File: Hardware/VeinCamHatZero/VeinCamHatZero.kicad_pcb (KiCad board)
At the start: 2 copper layers, 65 x 30 mm, 17 parts, among them J1 Raspberry_Pi_2_3, Q1 BSD235N

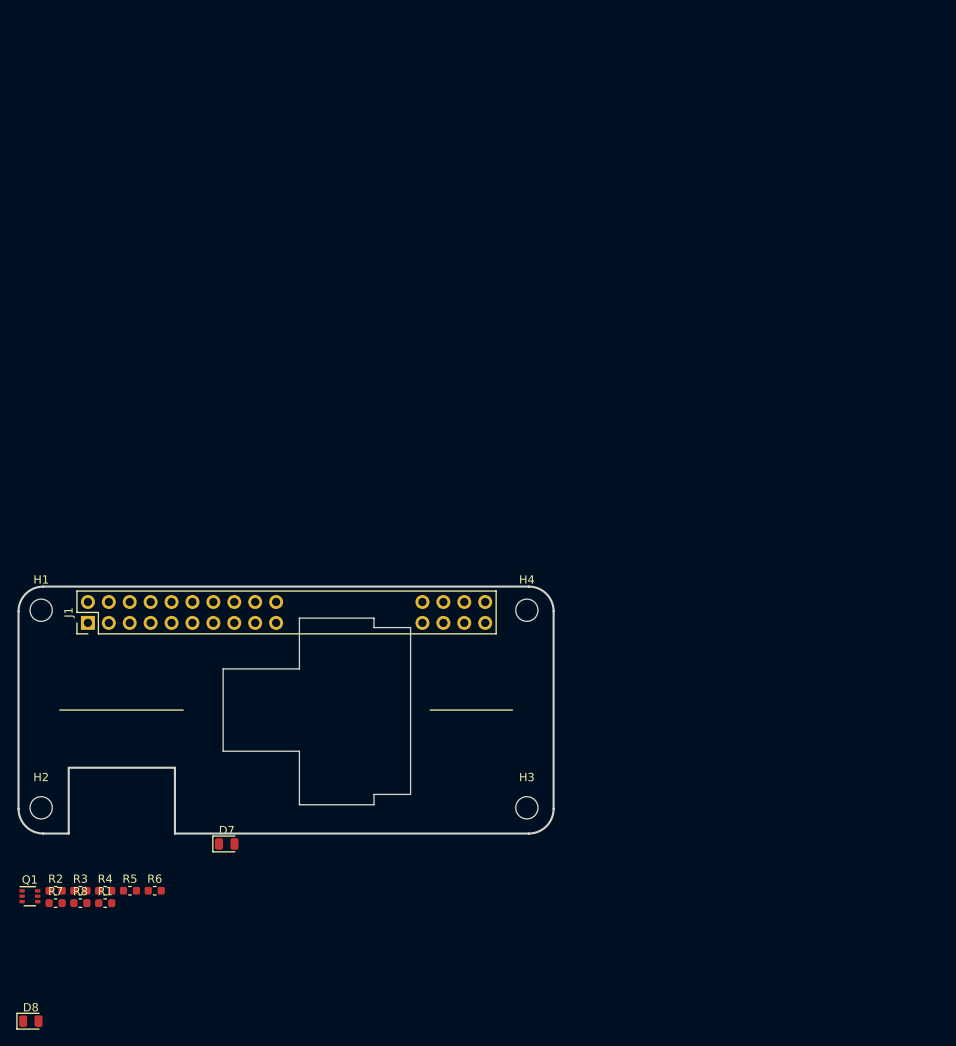
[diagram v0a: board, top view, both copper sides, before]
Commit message: Laid out VeinCamHatZero and added IR LED footprint/model
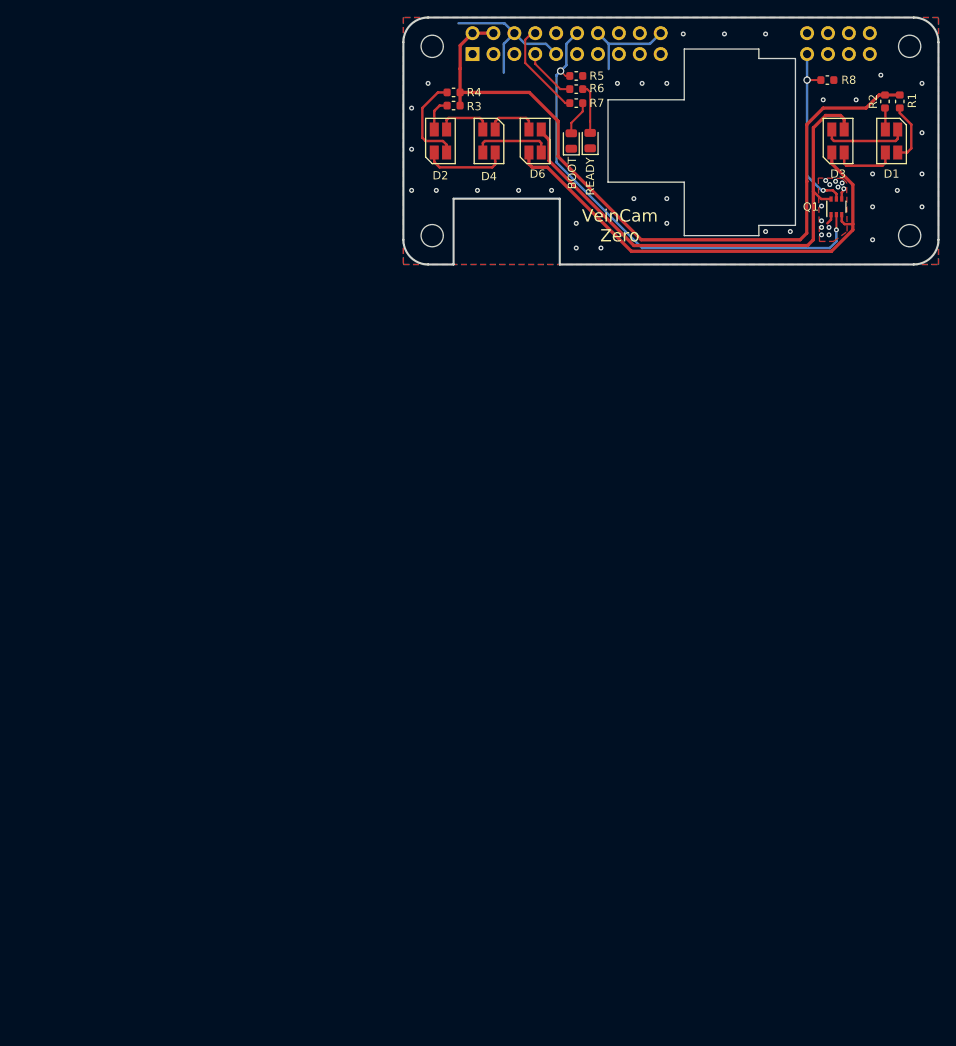
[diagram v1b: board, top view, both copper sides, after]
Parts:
- added D1: SFH7252, VeinCam_Footprints:SFH7252, F.Cu at (264.3, 80.0)
- added D2: SFH7252, VeinCam_Footprints:SFH7252, F.Cu at (209.5, 80.0)
- added D3: SFH7252, VeinCam_Footprints:SFH7252, F.Cu at (257.8, 80.0)
- added D4: SFH7252, VeinCam_Footprints:SFH7252, F.Cu at (215.4, 80.0)
- added D6: SFH7252, VeinCam_Footprints:SFH7252, F.Cu at (221.0, 80.0)
- moved R2 139.1 mm to (263.5, 75.2), turned to 90 degrees
- moved R1 137.1 mm to (265.3, 75.2), turned to 90 degrees
- moved R8 135.0 mm to (256.5, 72.6)
- moved Q1 128.9 mm to (257.6, 88.0), turned to 90 degrees
- moved D8 125.5 mm to (225.4, 80.0), turned to 90 degrees
- moved R7 116.0 mm to (226.0, 75.4)
- moved R5 112.9 mm to (226.0, 72.1)
- moved R6 110.0 mm to (226.0, 73.7)
- moved R4 105.8 mm to (211.1, 74.1)
- moved R3 105.6 mm to (211.1, 75.7)
- moved D7 96.2 mm to (227.7, 80.0), turned to 90 degrees
- moved H2 84.2 mm to (208.5, 91.5)
- moved H3 83.6 mm to (266.5, 91.5)
- moved TP1 83.5 mm to (205.0, 95.0)
- moved J1 83.4 mm to (213.4, 69.4)
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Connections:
- J1 pad 1: +3V3 -> Net-(J1-Pad1)
- J1 pad 12: Net-(J1-Pad12) -> /LED_940
- J1 pad 15: /LED_READY -> Net-(J1-Pad15)
- J1 pad 16: /LED_BOOT -> Net-(J1-Pad16)
- J1 pad 17: +3V3 -> Net-(J1-Pad17)
- J1 pad 7: Net-(J1-Pad7) -> /LED_READY
- J1 pad 8: Net-(J1-Pad8) -> /LED_BOOT
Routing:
- net +5V: track 0.00 -> 90.3 mm
- net Net-(D3-Pad3): track 0.00 -> 62.8 mm
- net /LED_940: track 0.00 -> 60.0 mm, vias 0 -> 2
- net Net-(D3-Pad1): track 0.00 -> 59.0 mm
- net GND: track 0.00 -> 33.0 mm, vias 0 -> 45
- net /LED_850: track 0.00 -> 21.6 mm, vias 0 -> 2
- net /LED_BOOT: track 0.00 -> 11.8 mm
- net Net-(D2-Pad4): track 0.00 -> 11.7 mm
- net Net-(D2-Pad1): track 0.00 -> 10.5 mm
- net Net-(D1-Pad1): track 0.00 -> 10.5 mm
- net Net-(D4-Pad3): track 0.00 -> 9.61 mm
- net Net-(D1-Pad3): track 0.00 -> 8.22 mm
- net Net-(D1-Pad2): track 0.00 -> 7.35 mm
- net Net-(D2-Pad3): track 0.00 -> 6.85 mm
- net /LED_READY: track 0.00 -> 6.66 mm
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- added copper zone on B.Cu, net GND
- added copper zone on F.Cu, net GND
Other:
- rule via_min_drill: 0.5 -> 0.3
- rule via_min_size: 0.8 -> 0.6
- board text added: "Alex Binos Chris Bodger Josh Johnson Tom Johnson Alex Ollman Pat Wilton"
- board text added: "BOOT"
- board text added: "READY"
- board text added: "VeinCam Zero"
- board text added: "VeinCam2019:"
- board text added: "github.com/chrisbodger/VeinCam2019"

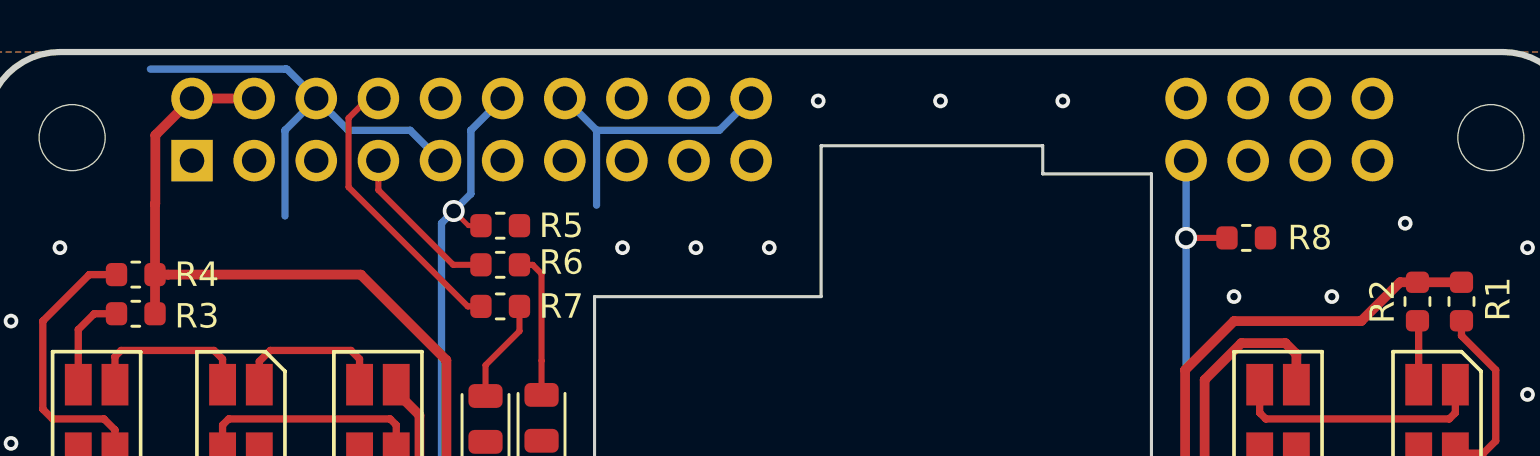
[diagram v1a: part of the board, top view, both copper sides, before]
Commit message: Added footprints for VeinCamHat and begun layout
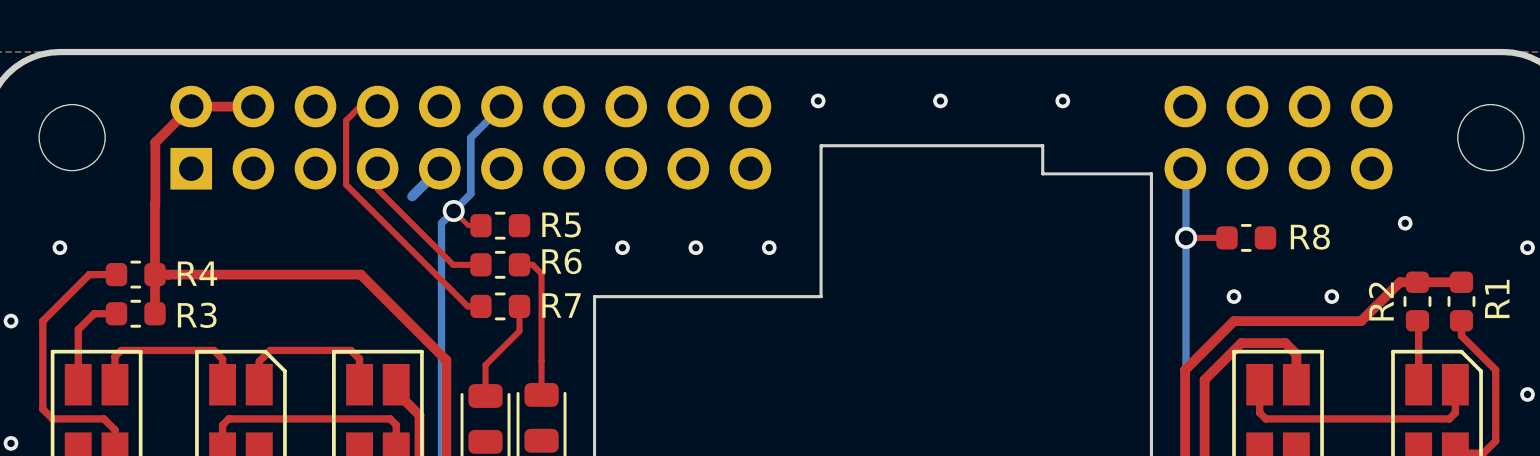
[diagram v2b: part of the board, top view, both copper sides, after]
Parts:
- moved J1 0.33 mm to (213.4, 69.8)
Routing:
- net GND: track 33.0 -> 4.15 mm

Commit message: Changes to renders
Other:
- board text added: "VeinCam"
- board text removed: "VeinCam Zero"
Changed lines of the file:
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@@
     (effects (font (size 1 1) (thickness 0.15)) (justify left mirror))
   )
-  (gr_text "VeinCam\nZero" (at 231.3 90.3) (layer F.SilkS)
+  (gr_text VeinCam (at 231.3 90.3) (layer F.SilkS)
     (effects (font (size 1.5 1.5) (thickness 0.3)))
   )

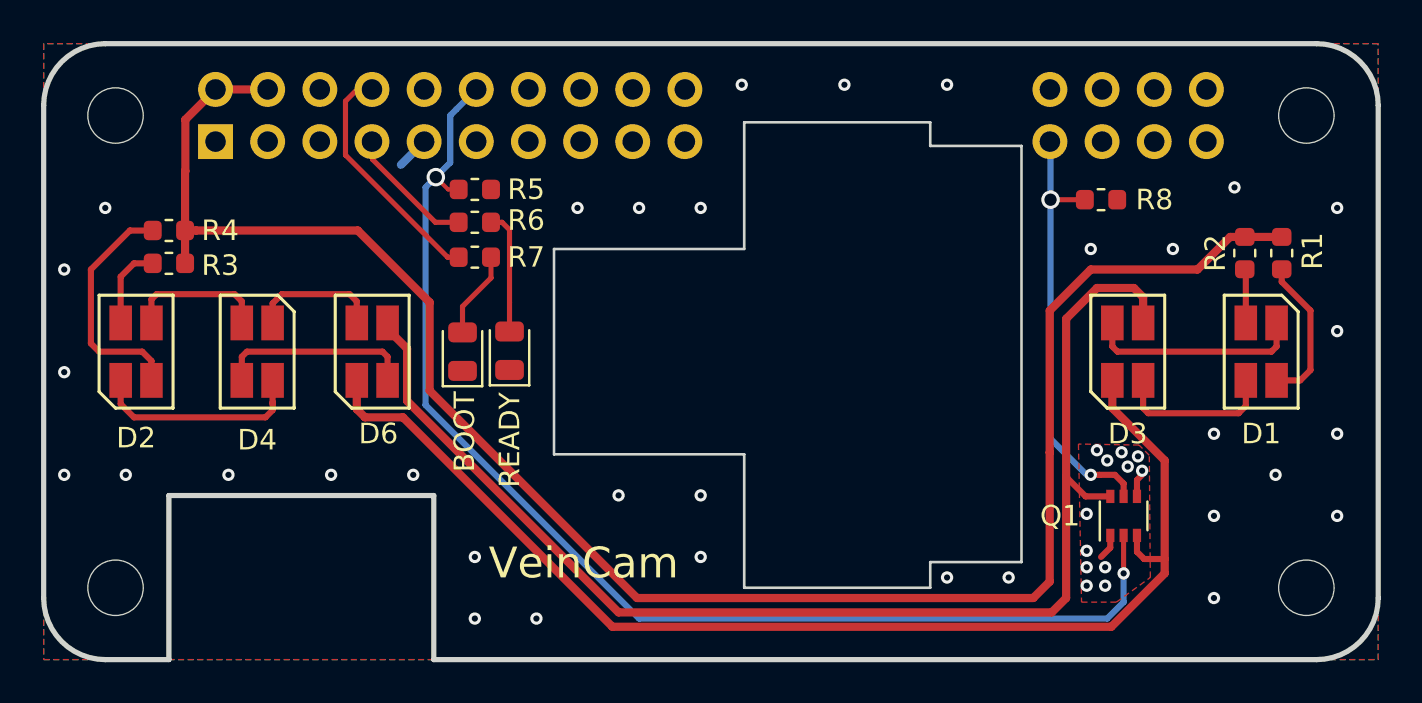
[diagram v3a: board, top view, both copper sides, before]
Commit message: Changed plans for VeinCam Plus, both boards laid out
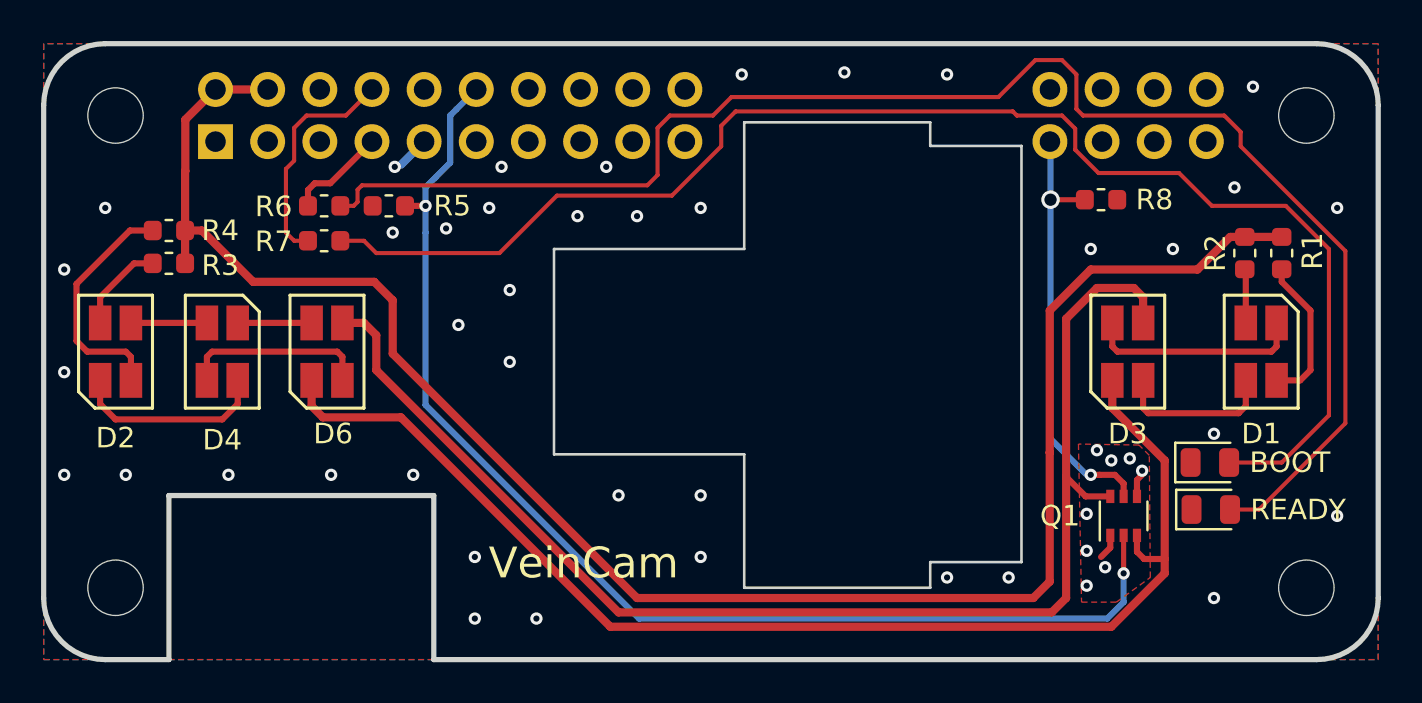
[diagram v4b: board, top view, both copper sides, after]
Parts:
- moved D8 36.8 mm to (261.8, 85.4), turned to 0 degrees
- moved D7 35.0 mm to (261.8, 87.7), turned to 0 degrees
- moved R7 7.38 mm to (218.7, 74.6)
- moved R6 7.38 mm to (218.7, 72.9)
- moved R5 4.26 mm to (221.8, 72.9), turned to 180 degrees
- moved D6 2.20 mm to (218.8, 80.0)
- moved D4 1.70 mm to (213.7, 80.0)
- moved D2 1.00 mm to (208.5, 80.0)
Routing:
- net Net-(D7-Pad2): track 6.01 -> 74.6 mm
- net Net-(D8-Pad2): track 4.24 -> 69.1 mm
- net Net-(D2-Pad3): track 6.85 -> 3.70 mm
- net Net-(D4-Pad1): track 6.43 -> 3.60 mm
- net Net-(D3-Pad1): track 59.0 -> 61.1 mm
- net /LED_READY: track 6.66 -> 4.83 mm
- net Net-(D3-Pad3): track 62.8 -> 64.3 mm
- net +5V: track 90.0 -> 89.0 mm
- net Net-(D2-Pad1): track 10.5 -> 9.62 mm
- net GND: vias 45 -> 47
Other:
- board text removed: "Alex Binos Chris Bodger Josh Johnson Tom Johnson Alex Ollman Pat Wilton"
- board text removed: "VeinCam2019:"
- board text removed: "github.com/chrisbodger/VeinCam2019"

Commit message: More Hardware changes, both boards complete
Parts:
- Q1: value BSD235N -> NTJD4001N
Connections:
- J1 pad 1: Net-(J1-Pad1) -> (no net)
- J1 pad 10: Net-(J1-Pad10) -> (no net)
- J1 pad 11: Net-(J1-Pad11) -> (no net)
- J1 pad 13: Net-(J1-Pad13) -> (no net)
- J1 pad 15: Net-(J1-Pad15) -> (no net)
- J1 pad 16: Net-(J1-Pad16) -> (no net)
- J1 pad 17: Net-(J1-Pad17) -> (no net)
- J1 pad 18: Net-(J1-Pad18) -> (no net)
- J1 pad 19: Net-(J1-Pad19) -> (no net)
- J1 pad 3: Net-(J1-Pad3) -> (no net)
- J1 pad 35: Net-(J1-Pad35) -> (no net)
- J1 pad 36: Net-(J1-Pad36) -> (no net)
- J1 pad 37: Net-(J1-Pad37) -> (no net)
- J1 pad 38: Net-(J1-Pad38) -> (no net)
- J1 pad 40: Net-(J1-Pad40) -> (no net)
- J1 pad 5: Net-(J1-Pad5) -> (no net)

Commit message: final board changes, gerbers generated
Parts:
- moved D3 1.20 mm to (259.0, 80.0)
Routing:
- net Net-(D1-Pad3): track 8.22 -> 6.37 mm
- net Net-(D1-Pad1): track 10.5 -> 9.25 mm
- net Net-(D3-Pad3): track 64.3 -> 65.1 mm
- net +5V: track 89.0 -> 88.5 mm
- net GND: vias 47 -> 49
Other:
- rule solder_mask_min_width: 0.25 -> 0.1
- board text added: "NOTE: 1mm Final Thickness, not 1.6mm"

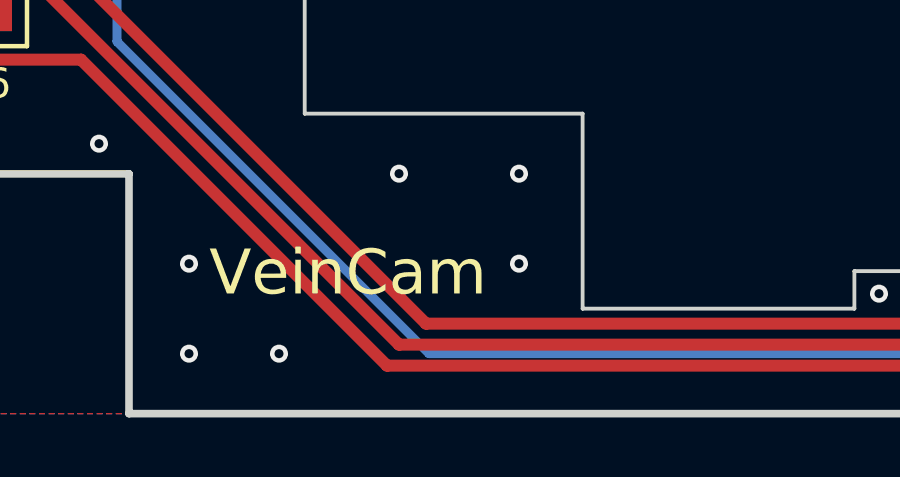
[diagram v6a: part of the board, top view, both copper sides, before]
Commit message: Finished boards, v0.2 gerbers zipped and sent off to fab
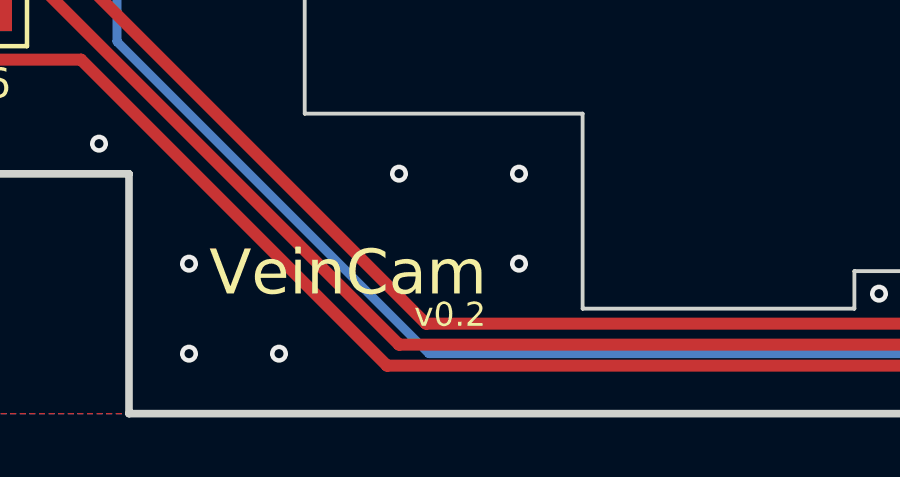
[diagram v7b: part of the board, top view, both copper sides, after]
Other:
- board text added: "v0.2"
- board text added: "veincam.org"
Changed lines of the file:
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@@
-(kicad_pcb (version 20171130) (host pcbnew "(5.0.2)-1")
+(kicad_pcb (version 20171130) (host pcbnew "(5.1.0)-1")
   (general
     (thickness 1)
-    (drawings 4)
+    (drawings 6)
     (tracks 237)
     (zones 0)
@@
     (zone_45_only no)
     (trace_min 0.1524)
-    (segment_width 0.1)
-    (edge_width 0.1)
     (via_size 0.9)
     (via_drill 0.6)
@@
     (uvia_min_size 0.5)
     (uvia_min_drill 0.1)
+    (edge_width 0.1)
+    (segment_width 0.1)
     (pcb_text_width 0.3)
     (pcb_text_size 1 1)
@@
     )
   )
+  (gr_text veincam.org (at 243.8 93) (layer B.SilkS)
+    (effects (font (size 1 1) (thickness 0.2)) (justify mirror))
+  )
+  (gr_text v0.2 (at 234.7 91.7) (layer F.SilkS)
+    (effects (font (size 0.8 0.8) (thickness 0.12)))
+  )
   (gr_text "NOTE: 1mm Final Thickness, not 1.6mm" (at 234.3 99.6) (layer Cmts.User)
